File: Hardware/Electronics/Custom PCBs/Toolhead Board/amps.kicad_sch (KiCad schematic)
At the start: 52 parts, among them Q1 MMBT4403, U4 HX711

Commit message: Work on toolhead board more
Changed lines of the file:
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@@
+    )
+  )
+  (symbol (lib_name "PWR_FLAG_1") (lib_id "power:PWR_FLAG") (at 76.2 21.59 0) (unit 1)
+    (in_bom yes) (on_board yes) (dnp no) (fields_autoplaced)
+    (property "Reference" "#FLG06" (at 76.2 19.685 0)
+      (effects (font (size 1.27 1.27)) hide)
+    )
+    (property "Value" "PWR_FLAG" (at 76.2 16.51 0)
+      (effects (font (size 1.27 1.27)))
+    )
+    (property "Footprint" "" (at 76.2 21.59 0)
+      (effects (font (size 1.27 1.27)) hide)
+    )
+    (property "Datasheet" "~" (at 76.2 21.59 0)
+      (effects (font (size 1.27 1.27)) hide)
+    )
+    (pin "1")
+    (instances
+      (project "Toolhead Board"
+        (path "/a1747683-152e-4245-ab61-2d33ce6021ef/fe3b39b1-861f-4ade-961f-d72da0b86b52"
+          (reference "#FLG06") (unit 1)
+        )
+      )
     )
   )

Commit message: Finish Toolhead Schematic
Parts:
- C12, C19, C22, C23: LCSC C1591 -> (none)
- C16, C18: LCSC C15850 -> (none)
- L1: LCSC C307744 -> (none)
- Q1: LCSC C78864 -> (none)
- R18, R19, R20, R21: Digikey (none) -> RMCF2512JT330RCT-ND; LCSC C19866 -> (none)
- R3: footprint Resistor_SMD:R_0603_1608Metric -> Resistor_SMD:R_0603_1608Metric_Pad0.98x0.95mm_HandSolder; Digikey RMCF0603JT10K0CT-ND -> 1292-WR06X103JTLCT-ND; LCSC C98220 -> (none); Mouser 652-CR0603FX-1002ELF -> (none)
- R4: footprint Resistor_SMD:R_0603_1608Metric -> Resistor_SMD:R_0603_1608Metric_Pad0.98x0.95mm_HandSolder; Digikey RMCF0603FT8K20CT-ND -> 311-8.2KGRCT-ND; LCSC C114637 -> (none); Mouser 652-CR0603FX-8201ELF -> (none)
- R5, R6: footprint Resistor_SMD:R_0603_1608Metric -> Resistor_SMD:R_0603_1608Metric_Pad0.98x0.95mm_HandSolder; Digikey RMCF0603FT100RCT-ND -> 311-100HRCT-ND; LCSC C319953 -> (none); Mouser 652-CR0603FX-1000ELF -> (none)
- U4: LCSC C43656 -> (none)

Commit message: Updated Footprints
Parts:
- C12, C19, C22, C23: footprint Capacitor_SMD:C_0603_1608Metric -> Capacitor_SMD:C_0603_1608Metric_Pad1.08x0.95mm_HandSolder

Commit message: Update toolhead board layout
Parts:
- C12, C19, C22, C23: footprint Capacitor_SMD:C_0603_1608Metric -> Capacitor_SMD:C_0603_1608Metric_Pad1.08x0.95mm_HandSolder
- C16, C18: footprint Capacitor_SMD:C_0805_2012Metric -> Capacitor_SMD:C_0805_2012Metric_Pad1.18x1.45mm_HandSolder
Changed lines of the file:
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@@
 			)
 		)
-		(property "Footprint" "Capacitor_SMD:C_0805_2012Metric"
+		(property "Footprint" "Capacitor_SMD:C_0805_2012Metric_Pad1.18x1.45mm_HandSolder"
 			(at 45.72 142.24 0)
 			(effects
@@
 			)
 		)
-		(property "Footprint" "Capacitor_SMD:C_0603_1608Metric"
+		(property "Footprint" "Capacitor_SMD:C_0603_1608Metric_Pad1.08x0.95mm_HandSolder"
 			(at 74.93 107.95 0)
 			(effects
@@
 			)
 		)
-		(property "Footprint" "Capacitor_SMD:C_0805_2012Metric"
+		(property "Footprint" "Capacitor_SMD:C_0805_2012Metric_Pad1.18x1.45mm_HandSolder"
 			(at 44.45 82.55 0)
 			(effects
@@
 			)
 		)
-		(property "Footprint" "Capacitor_SMD:C_0603_1608Metric"
+		(property "Footprint" "Capacitor_SMD:C_0603_1608Metric_Pad1.08x0.95mm_HandSolder"
 			(at 53.34 82.55 0)
 			(effects
@@
 			)
 		)
-		(property "Footprint" "Capacitor_SMD:C_0805_2012Metric"
+		(property "Footprint" "Capacitor_SMD:C_0805_2012Metric_Pad1.18x1.45mm_HandSolder"
 			(at 30.48 43.18 0)
 			(effects
@@
 			)
 		)
-		(property "Footprint" "Capacitor_SMD:C_0603_1608Metric"
+		(property "Footprint" "Capacitor_SMD:C_0603_1608Metric_Pad1.08x0.95mm_HandSolder"
 			(at 76.2 167.64 0)
 			(effects
@@
 			)
 		)
-		(property "Footprint" "Capacitor_SMD:C_0603_1608Metric"
+		(property "Footprint" "Capacitor_SMD:C_0603_1608Metric_Pad1.08x0.95mm_HandSolder"
 			(at 67.31 124.46 0)
 			(effects
@@
 			)
 		)
-		(property "Footprint" "Capacitor_SMD:C_0603_1608Metric"
+		(property "Footprint" "Capacitor_SMD:C_0603_1608Metric_Pad1.08x0.95mm_HandSolder"
 			(at 40.64 161.29 0)
 			(effects
@@
 			)
 		)
-		(property "Footprint" "Capacitor_SMD:C_0805_2012Metric"
+		(property "Footprint" "Capacitor_SMD:C_0805_2012Metric_Pad1.18x1.45mm_HandSolder"
 			(at 44.45 24.13 0)
 			(effects
@@
 			)
 		)
-		(property "Footprint" "Capacitor_SMD:C_0805_2012Metric"
+		(property "Footprint" "Capacitor_SMD:C_0805_2012Metric_Pad1.18x1.45mm_HandSolder"
 			(at 30.48 101.6 0)
 			(effects
@@
 			)
 		)
-		(property "Footprint" "Capacitor_SMD:C_0603_1608Metric"
+		(property "Footprint" "Capacitor_SMD:C_0603_1608Metric_Pad1.08x0.95mm_HandSolder"
 			(at 68.58 184.15 0)
 			(effects
@@
 			)
 		)
-		(property "Footprint" "Capacitor_SMD:C_0603_1608Metric"
+		(property "Footprint" "Capacitor_SMD:C_0603_1608Metric_Pad1.08x0.95mm_HandSolder"
 			(at 54.61 142.24 0)
 			(effects
@@
 			)
 		)
-		(property "Footprint" "Capacitor_SMD:C_0603_1608Metric"
+		(property "Footprint" "Capacitor_SMD:C_0603_1608Metric_Pad1.08x0.95mm_HandSolder"
 			(at 39.37 101.6 0)
 			(effects
@@
 			)
 		)
-		(property "Footprint" "Capacitor_SMD:C_0805_2012Metric"
+		(property "Footprint" "Capacitor_SMD:C_0805_2012Metric_Pad1.18x1.45mm_HandSolder"
 			(at 31.75 161.29 0)
 			(effects

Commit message: Update layout
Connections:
- net +3V3 renamed +3.3V
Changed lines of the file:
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@@
 	)
 	(symbol
-		(lib_id "power:+3.3V")
-		(at 62.23 137.16 0)
-		(unit 1)
-		(exclude_from_sim no)
-		(in_bom yes)
-		(on_board yes)
-		(dnp no)
-		(property "Reference" "#PWR0116"
-			(at 62.23 140.97 0)
-			(effects
-				(font
-					(size 1.27 1.27)
-				)
-				(hide yes)
-			)
-		)
-		(property "Value" "+3V3"
-			(at 62.611 132.7658 0)
-			(effects
-				(font
-					(size 1.27 1.27)
-				)
-			)
-		)
-		(property "Footprint" ""
-			(at 62.23 137.16 0)
-			(effects
-				(font
-					(size 1.27 1.27)
-				)
-				(hide yes)
-			)
-		)
-		(property "Datasheet" ""
-			(at 62.23 137.16 0)
-			(effects
-				(font
-					(size 1.27 1.27)
-				)
-				(hide yes)
-			)
-		)
-		(property "Description" ""
-			(at 62.23 137.16 0)
-			(effects
-				(font
-					(size 1.27 1.27)
-				)
-				(hide yes)
-			)
-		)
-		(pin "1"
-		)
-		(instances
-			(project "view_base"
-				(path "/5edcefbe-9766-42c8-9529-28d0ec865573"
-					(reference "#PWR0116")
-					(unit 1)
-				)
-			)
-			(project "Toolhead Board"
-				(path "/a1747683-152e-4245-ab61-2d33ce6021ef/fe3b39b1-861f-4ade-961f-d72da0b86b52"
-					(reference "#PWR085")
-					(unit 1)
-				)
-			)
-		)
-	)
-	(symbol
 		(lib_id "Device:R_Small")
 		(at 45.72 127 90)
@@
 	)
 	(symbol
-		(lib_id "power:+3.3V")
-		(at 60.96 19.05 0)
-		(unit 1)
-		(exclude_from_sim no)
-		(in_bom yes)
-		(on_board yes)
-		(dnp no)
-		(property "Reference" "#PWR0116"
-			(at 60.96 22.86 0)
-			(effects
-				(font
-					(size 1.27 1.27)
-				)
-				(hide yes)
-			)
-		)
-		(property "Value" "+3V3"
-			(at 61.341 14.6558 0)
-			(effects
-				(font
-					(size 1.27 1.27)
-				)
-			)
-		)
-		(property "Footprint" ""
-			(at 60.96 19.05 0)
-			(effects
-				(font
-					(size 1.27 1.27)
-				)
-				(hide yes)
-			)
-		)
-		(property "Datasheet" ""
-			(at 60.96 19.05 0)
-			(effects
-				(font
-					(size 1.27 1.27)
-				)
-				(hide yes)
-			)
-		)
-		(property "Description" ""
-			(at 60.96 19.05 0)
-			(effects
-				(font
-					(size 1.27 1.27)
-				)
-				(hide yes)
-			)
-		)
-		(pin "1"
-		)
-		(instances
-			(project "view_base"
-				(path "/5edcefbe-9766-42c8-9529-28d0ec865573"
-					(reference "#PWR0116")
-					(unit 1)
-				)
-			)
-			(project "Toolhead Board"
-				(path "/a1747683-152e-4245-ab61-2d33ce6021ef/fe3b39b1-861f-4ade-961f-d72da0b86b52"
-					(reference "#PWR067")
-					(unit 1)
-				)
-			)
-		)
-	)
-	(symbol
 		(lib_id "power:GNDA")
 		(at 105.41 55.88 0)
@@
 	)
 	(symbol
+		(lib_id "power:+3.3V")
+		(at 60.96 19.05 0)
+		(unit 1)
+		(exclude_from_sim no)
+		(in_bom yes)
+		(on_board yes)
+		(dnp no)
+		(fields_autoplaced yes)
+		(property "Reference" "#PWR047"
+			(at 60.96 22.86 0)
+			(effects
+				(font
+					(size 1.27 1.27)
+				)
+				(hide yes)
+			)
+		)
+		(property "Value" "+3.3V"
+			(at 60.96 13.97 0)
+			(effects
+				(font
+					(size 1.27 1.27)
+				)
+			)
+		)
+		(property "Footprint" ""
+			(at 60.96 19.05 0)
+			(effects
+				(font
+					(size 1.27 1.27)
+				)
+				(hide yes)
+			)
+		)
+		(property "Datasheet" ""
+			(at 60.96 19.05 0)
+			(effects
+				(font
+					(size 1.27 1.27)
+				)
+				(hide yes)
+			)
+		)
+		(property "Description" ""
+			(at 60.96 19.05 0)
+			(effects
+				(font
+					(size 1.27 1.27)
+				)
+				(hide yes)
+			)
+		)
+		(pin "1"
+		)
+		(instances
+			(project "Toolhead Board"
+				(path "/a1747683-152e-4245-ab61-2d33ce6021ef/fe3b39b1-861f-4ade-961f-d72da0b86b52"
+					(reference "#PWR047")
+					(unit 1)
+				)
+			)
+		)
+	)
+	(symbol
 		(lib_id "Device:R_Small")
 		(at 46.99 181.61 270)
@@
 	)
 	(symbol
-		(lib_id "power:+3.3V")
-		(at 60.96 77.47 0)
+		(lib_id "power:GNDA")
+		(at 113.03 157.48 0)
 		(unit 1)
 		(exclude_from_sim no)
@@
 		(on_board yes)
 		(dnp no)
-		(property "Reference" "#PWR0116"
-			(at 60.96 81.28 0)
+		(property "Reference" "#PWR0125"
+			(at 113.03 163.83 0)
 			(effects
 				(font
@@
 			)
 		)
-		(property "Value" "+3V3"
-			(at 61.341 73.0758 0)
+		(property "Value" "GNDA"
+			(at 113.157 161.8742 0)
 			(effects
 				(font
@@
 		)
 		(property "Footprint" ""
-			(at 60.96 77.47 0)
+			(at 113.03 157.48 0)
 			(effects
 				(font
@@
 		)
 		(property "Datasheet" ""
-			(at 60.96 77.47 0)
+			(at 113.03 157.48 0)
 			(effects
 				(font
@@
 		)
 		(property "Description" ""
-			(at 60.96 77.47 0)
+			(at 113.03 157.48 0)
 			(effects
 				(font
@@
 			(project "view_base"
 				(path "/5edcefbe-9766-42c8-9529-28d0ec865573"
-					(reference "#PWR0116")
+					(reference "#PWR0125")
 					(unit 1)
 				)
@@
 			(project "Toolhead Board"
 				(path "/a1747683-152e-4245-ab61-2d33ce6021ef/fe3b39b1-861f-4ade-961f-d72da0b86b52"
-					(reference "#PWR077")
+					(reference "#PWR087")
 					(unit 1)
 				)
@@
 	)
 	(symbol
-		(lib_id "power:GNDA")
-		(at 113.03 157.48 0)
+		(lib_id "power:+3.3V")
+		(at 62.23 137.16 0)
 		(unit 1)
 		(exclude_from_sim no)
@@
 		(on_board yes)
 		(dnp no)
-		(property "Reference" "#PWR0125"
-			(at 113.03 163.83 0)
+		(fields_autoplaced yes)
+		(property "Reference" "#PWR077"
+			(at 62.23 140.97 0)
 			(effects
 				(font
@@
 			)
 		)
-		(property "Value" "GNDA"
-			(at 113.157 161.8742 0)
+		(property "Value" "+3.3V"
+			(at 62.23 132.08 0)
 			(effects
 				(font
@@
 		)
 		(property "Footprint" ""
-			(at 113.03 157.48 0)
+			(at 62.23 137.16 0)
 			(effects
 				(font
@@
 		)
 		(property "Datasheet" ""
-			(at 113.03 157.48 0)
+			(at 62.23 137.16 0)
 			(effects
 				(font
@@
 		)
 		(property "Description" ""
-			(at 113.03 157.48 0)
+			(at 62.23 137.16 0)
 			(effects
 				(font
@@
 		)
 		(instances
-			(project "view_base"
-				(path "/5edcefbe-9766-42c8-9529-28d0ec865573"
-					(reference "#PWR0125")
-					(unit 1)
-				)
-			)
 			(project "Toolhead Board"
 				(path "/a1747683-152e-4245-ab61-2d33ce6021ef/fe3b39b1-861f-4ade-961f-d72da0b86b52"
-					(reference "#PWR087")
+					(reference "#PWR077")
 					(unit 1)
 				)
@@
 					(unit 1)
 				)
+			)
+		)
+	)
+	(symbol
+		(lib_id "power:+3.3V")
+		(at 60.96 77.47 0)
+		(unit 1)
+		(exclude_from_sim no)
+		(in_bom yes)
+		(on_board yes)
+		(dnp no)
+		(fields_autoplaced yes)
+		(property "Reference" "#PWR067"
+			(at 60.96 81.28 0)
+			(effects
+				(font
+					(size 1.27 1.27)
+				)
+				(hide yes)
+			)
+		)
+		(property "Value" "+3.3V"
+			(at 60.96 72.39 0)
+			(effects
+				(font
+					(size 1.27 1.27)
+				)
+			)
+		)
+		(property "Footprint" ""
+			(at 60.96 77.47 0)
+			(effects
+				(font
+					(size 1.27 1.27)
+				)
+				(hide yes)
+			)
+		)
+		(property "Datasheet" ""
+			(at 60.96 77.47 0)
+			(effects
+				(font
+					(size 1.27 1.27)
+				)
+				(hide yes)
+			)
+		)
+		(property "Description" ""
+			(at 60.96 77.47 0)
+			(effects
+				(font
+					(size 1.27 1.27)
+				)
+				(hide yes)
+			)
+		)
+		(pin "1"
+		)
+		(instances
+			(project "Toolhead Board"
+				(path "/a1747683-152e-4245-ab61-2d33ce6021ef/fe3b39b1-861f-4ade-961f-d72da0b86b52"
+					(reference "#PWR067")
+					(unit 1)
+				)

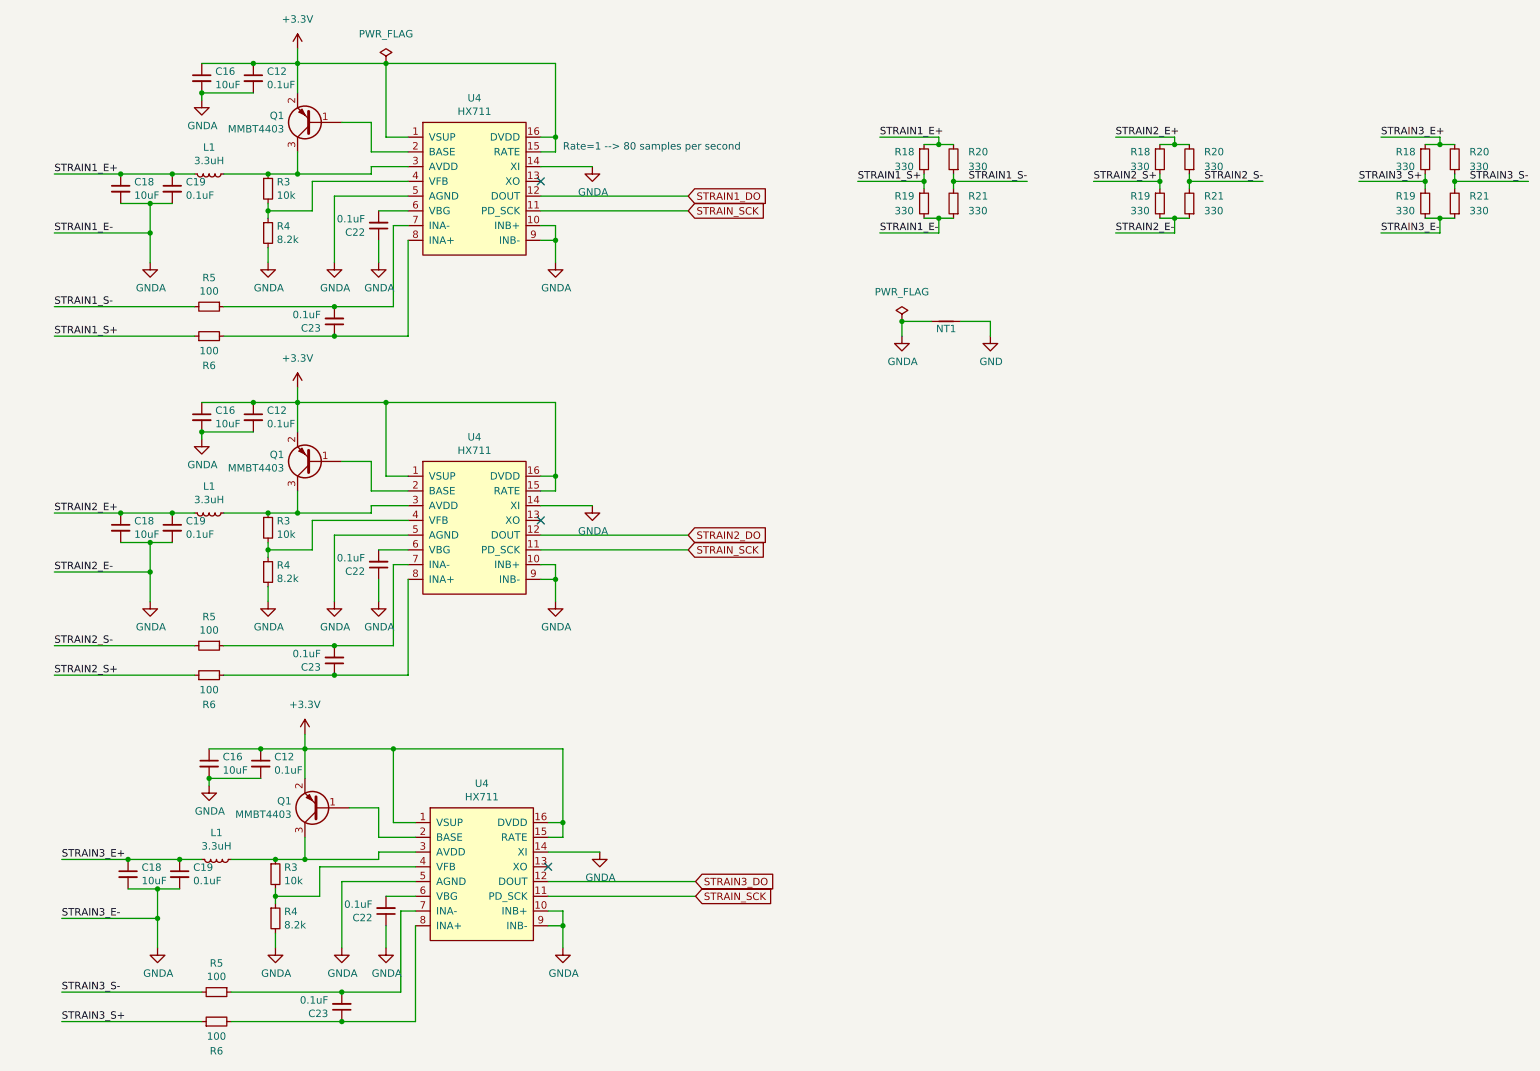
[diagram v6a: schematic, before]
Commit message: Update toolhead schematic+layout and add tolerances to base
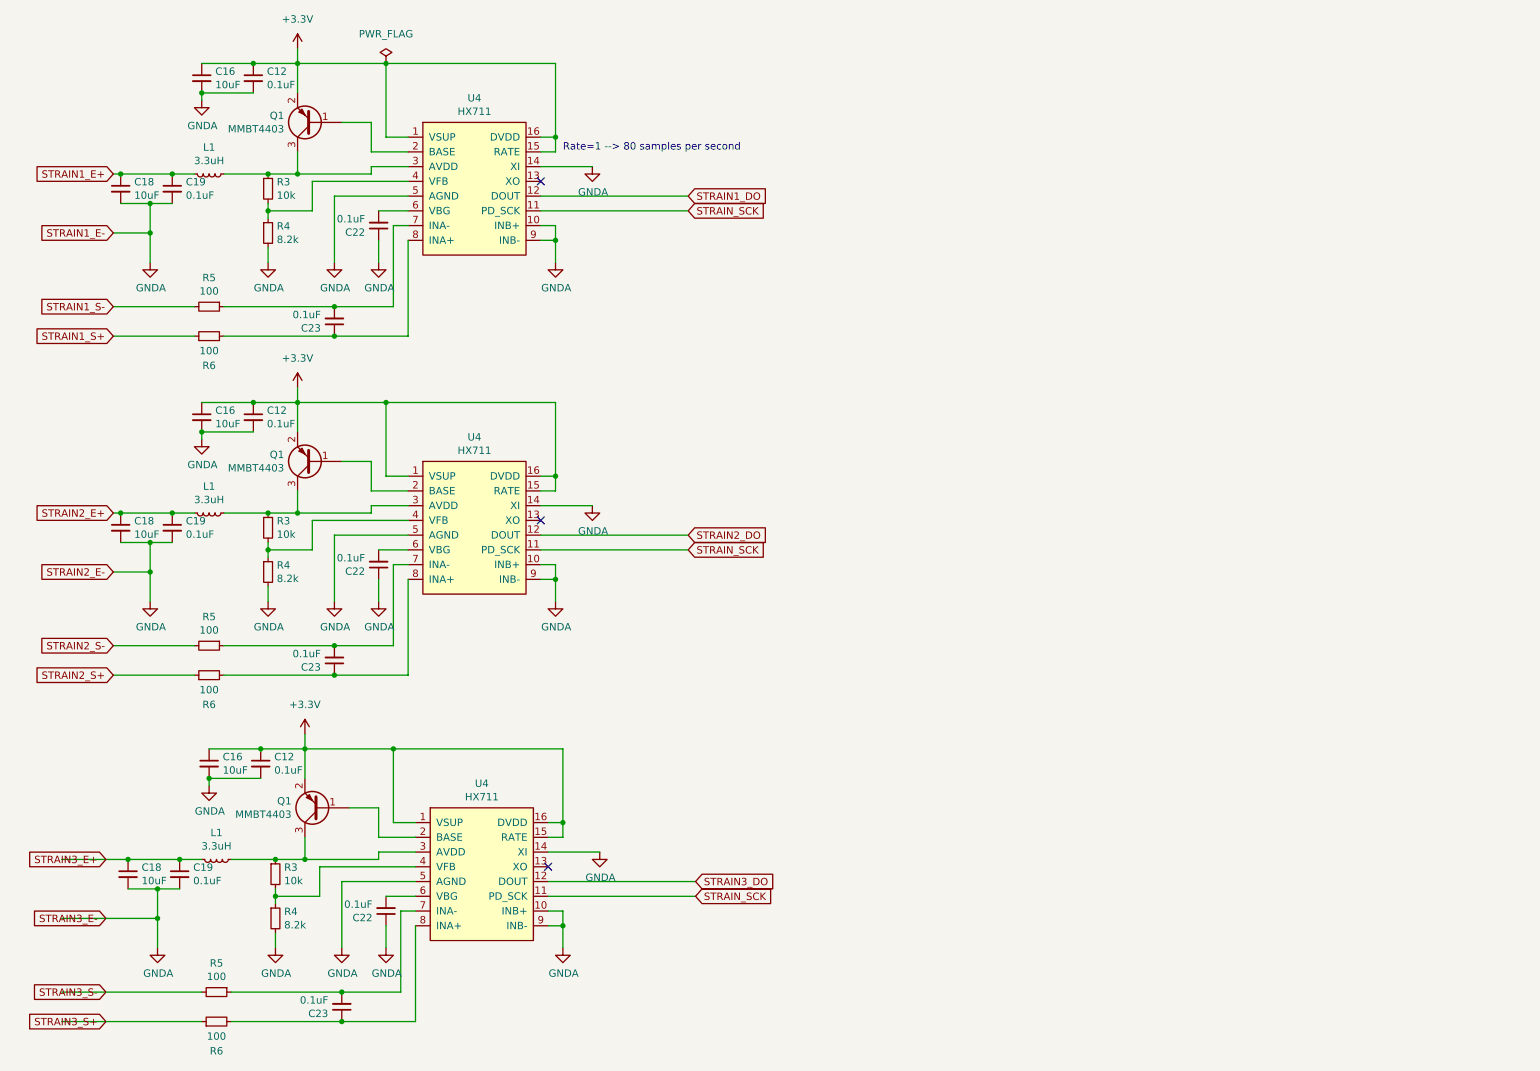
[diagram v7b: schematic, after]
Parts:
- removed NT1: NetTie_2, NetTie:NetTie-2_SMD_Pad0.5mm, symbol Device:NetTie_2
- removed R18 (x3), R19 (x3), R20 (x3), R21 (x3): 330, Resistor_SMD:R_2512_6332Metric, symbol Device:R_Small

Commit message: Update toolhead PCB layout
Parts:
- added NT1, NT2, NT3: NetTie_2, NetTie:NetTie-2_SMD_Pad0.5mm, symbol Device:NetTie_2
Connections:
- removed net GNDA: C12.2, C12.2, C12.2, C16.2, C16.2, C16.2, C18.2, C18.2, C18.2, C19.2, C19.2, C19.2, C22.1, C22.1, C22.1, R4.2, R4.2, R4.2, U4.10 (INB+), U4.10 (INB+), U4.10 (INB+), U4.14 (XI), U4.14 (XI), U4.14 (XI), U4.5 (AGND), U4.5 (AGND), U4.5 (AGND), U4.9 (INB-), U4.9 (INB-), U4.9 (INB-)
- new net GND: NT1.2, NT2.2, NT3.2
- new net GND1: C12.2, C16.2, C18.2, C19.2, C22.1, NT1.1, R4.2, U4.10 (INB+), U4.14 (XI), U4.5 (AGND), U4.9 (INB-)
- new net GND2: C12.2, C16.2, C18.2, C19.2, C22.1, NT2.1, R4.2, U4.10 (INB+), U4.14 (XI), U4.5 (AGND), U4.9 (INB-)
- new net GND3: C12.2, C16.2, C18.2, C19.2, C22.1, NT3.1, R4.2, U4.10 (INB+), U4.14 (XI), U4.5 (AGND), U4.9 (INB-)
